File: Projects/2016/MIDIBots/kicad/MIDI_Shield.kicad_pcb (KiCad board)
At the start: 2 copper layers, 86.4 x 77.5 mm, 71 parts, among them IC1 PC900V, K1 SRVO1, K2 SRVO2, K3 SRVO3, P10 A3, P11 A4, P12 AUX_12V, P13 AUX_12V, P14 AUX_5V, P15 AUX_5V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

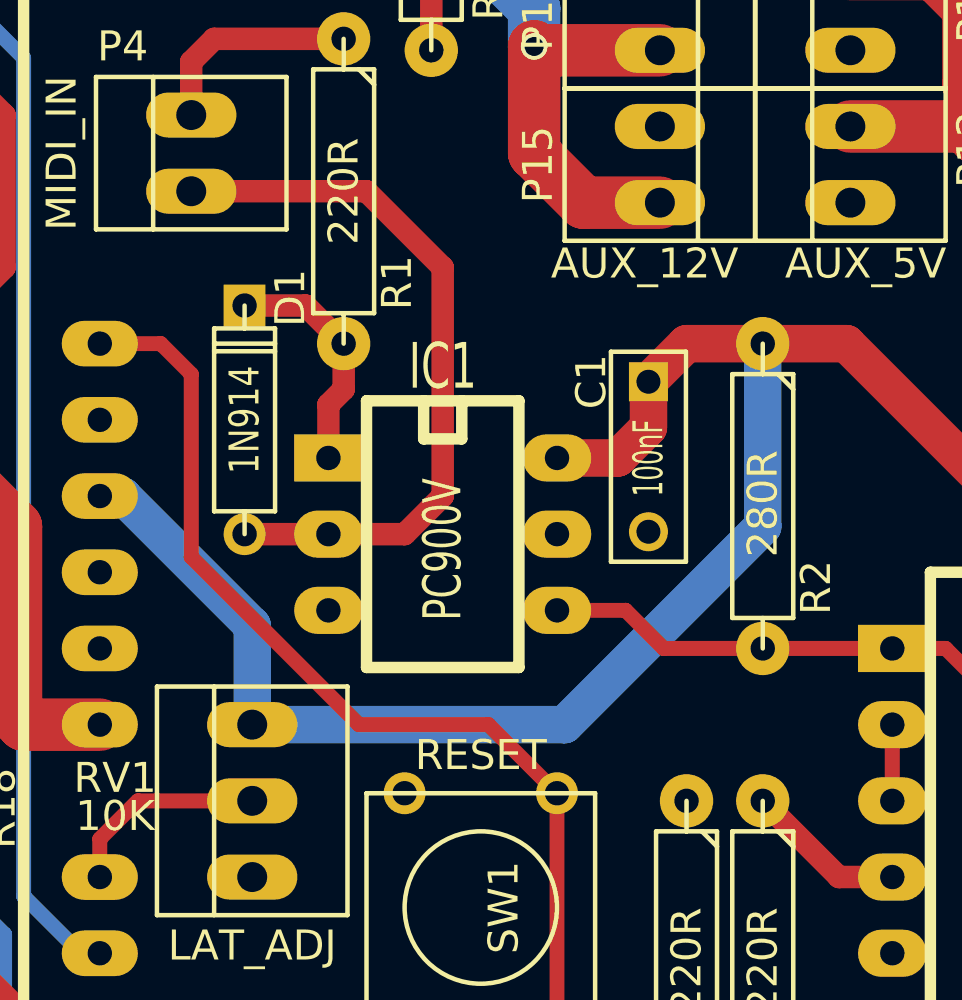
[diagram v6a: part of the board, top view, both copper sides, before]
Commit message: Added missing Vcc connection to MIDI thru output (and attendant rerouting)
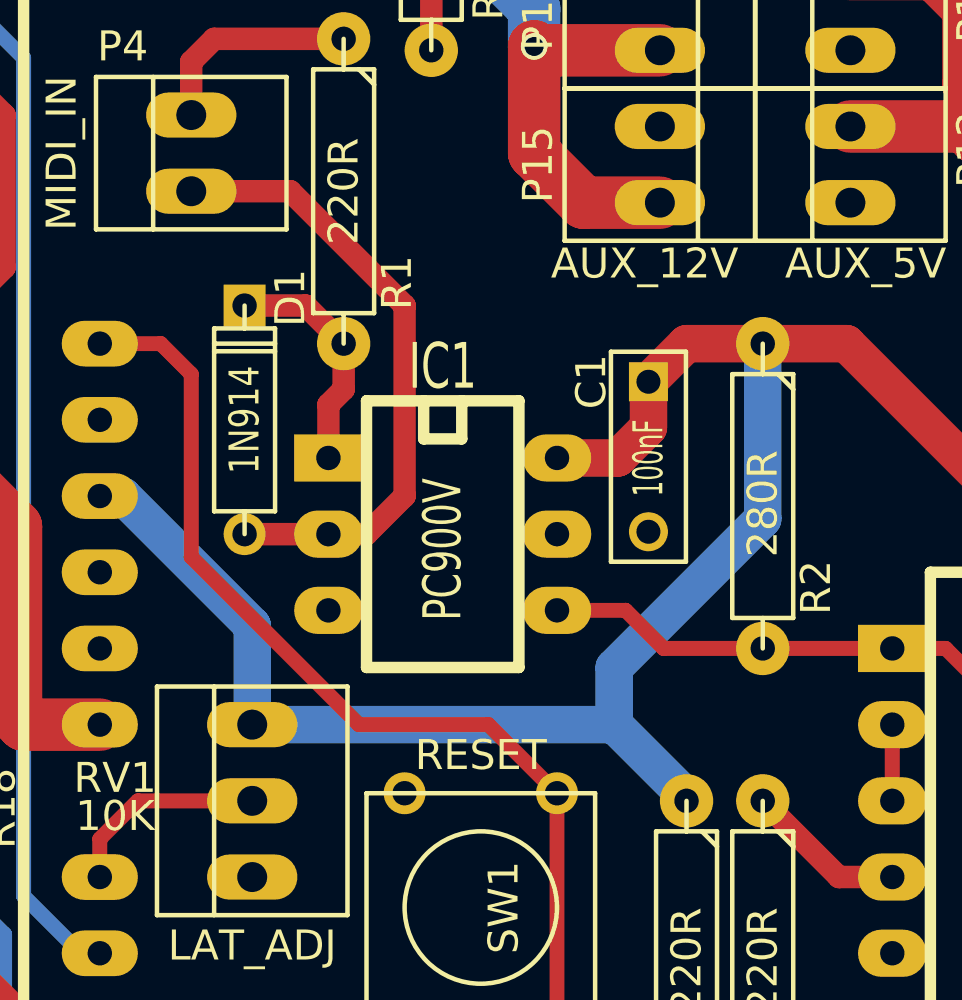
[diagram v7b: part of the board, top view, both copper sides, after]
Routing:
- net VCC: track 66.0 -> 70.6 mm
- net Net-(D1-Pad2): track 24.2 -> 20.9 mm
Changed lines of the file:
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@@
   (general
     (links 151)
-    (no_connects 1)
+    (no_connects 0)
     (area 50.749999 68.529999 143.560001 151.180001)
     (thickness 1.6)
     (drawings 22)
-    (tracks 270)
+    (tracks 273)
     (zones 0)
     (modules 71)
@@
   (segment (start 110.49 112.014) (end 110.49 110.998) (width 0.5) (layer F.Cu) (net 21))
   (segment (start 100.076 127) (end 100.076 129.54) (width 0.5) (layer F.Cu) (net 22))
-  (segment (start 78.74 127) (end 89.154 127) (width 1.25) (layer B.Cu) (net 23))
-  (segment (start 95.758 120.396) (end 95.758 114.3) (width 1.25) (layer B.Cu) (net 23))
-  (segment (start 89.154 127) (end 95.758 120.396) (width 1.25) (layer B.Cu) (net 23))
+  (segment (start 95.758 114.3) (end 95.758 120.142) (width 1.25) (layer B.Cu) (net 23) (status 400000))
+  (segment (start 90.805 125.095) (end 90.805 127) (width 1.25) (layer B.Cu) (net 23))
+  (segment (start 95.758 120.142) (end 90.805 125.095) (width 1.25) (layer B.Cu) (net 23))
+  (segment (start 93.218 129.54) (end 93.218 129.413) (width 1.25) (layer B.Cu) (net 23) (status C00000))
+  (segment (start 93.218 129.413) (end 90.805 127) (width 1.25) (layer B.Cu) (net 23) (status 400000))
+  (segment (start 90.805 127) (end 78.74 127) (width 1.25) (layer B.Cu) (net 23) (status 800000))
   (segment (start 73.66 119.38) (end 74.422 119.38) (width 1.25) (layer B.Cu) (net 23))
   (segment (start 74.422 119.38) (end 78.74 123.698) (width 1.25) (layer B.Cu) (net 23))
@@
   (segment (start 81.28 116.332) (end 81.28 118.11) (width 0.75) (layer F.Cu) (net 33))
   (segment (start 81.788 115.824) (end 81.28 116.332) (width 0.75) (layer F.Cu) (net 33))
+  (segment (start 76.708 109.22) (end 80.01 109.22) (width 0.75) (layer F.Cu) (net 34))
+  (segment (start 82.55 120.65) (end 81.28 120.65) (width 0.75) (layer F.Cu) (net 34))
+  (segment (start 83.82 119.38) (end 82.55 120.65) (width 0.75) (layer F.Cu) (net 34))
+  (segment (start 83.82 113.03) (end 83.82 119.38) (width 0.75) (layer F.Cu) (net 34))
+  (segment (start 80.01 109.22) (end 83.82 113.03) (width 0.75) (layer F.Cu) (net 34))
   (segment (start 78.486 120.65) (end 81.28 120.65) (width 0.75) (layer F.Cu) (net 34))
-  (segment (start 76.708 109.22) (end 82.55 109.22) (width 0.75) (layer F.Cu) (net 34))
-  (segment (start 83.82 120.65) (end 81.28 120.65) (width 0.75) (layer F.Cu) (net 34))
-  (segment (start 85.09 119.38) (end 83.82 120.65) (width 0.75) (layer F.Cu) (net 34))
-  (segment (start 85.09 111.76) (end 85.09 119.38) (width 0.75) (layer F.Cu) (net 34))
-  (segment (start 82.55 109.22) (end 85.09 111.76) (width 0.75) (layer F.Cu) (net 34))
   (segment (start 116.84 96.52) (end 116.84 98.298) (width 0.75) (layer F.Cu) (net 35))
   (segment (start 116.84 98.298) (end 119.888 101.346) (width 0.75) (layer F.Cu) (net 35))
@@
   (segment (start 123.571 112.776) (end 124.46 111.887) (width 0.5) (layer F.Cu) (net 45))
   (segment (start 127.635 102.87) (end 127.889 102.87) (width 0.5) (layer F.Cu) (net 45))
-  (segment (start 73.66 134.62) (end 73.025 134.62) (width 0.5) (layer B.Cu) (net 46) (status C00000))
-  (segment (start 73.025 134.62) (end 71.12 132.715) (width 0.5) (layer B.Cu) (net 46) (status 400000))
+  (segment (start 73.66 134.62) (end 73.025 134.62) (width 0.5) (layer B.Cu) (net 46))
+  (segment (start 73.025 134.62) (end 71.12 132.715) (width 0.5) (layer B.Cu) (net 46))
   (segment (start 71.12 132.715) (end 71.12 104.775) (width 0.5) (layer B.Cu) (net 46))
-  (segment (start 71.12 104.775) (end 68.58 102.235) (width 0.5) (layer B.Cu) (net 46) (status 800000))
-  (segment (start 73.66 137.16) (end 71.755 137.16) (width 0.5) (layer B.Cu) (net 47) (status 400000))
-  (segment (start 70.485 133.985) (end 68.58 132.08) (width 0.5) (layer B.Cu) (net 47) (status 800000))
+  (segment (start 71.12 104.775) (end 68.58 102.235) (width 0.5) (layer B.Cu) (net 46))
+  (segment (start 73.66 137.16) (end 71.755 137.16) (width 0.5) (layer B.Cu) (net 47))
+  (segment (start 70.485 133.985) (end 68.58 132.08) (width 0.5) (layer B.Cu) (net 47))
   (segment (start 70.485 135.89) (end 70.485 133.985) (width 0.5) (layer B.Cu) (net 47))
   (segment (start 71.755 137.16) (end 70.485 135.89) (width 0.5) (layer B.Cu) (net 47))
